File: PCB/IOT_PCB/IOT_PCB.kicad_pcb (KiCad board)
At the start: 2 copper layers, 6 parts, among them J1 Screw_Terminal_01x02, J2 Screw_Terminal_01x02, U1 ESP32-S3-WROOM-1, U2 BME280, U3 SCD41-D-R2

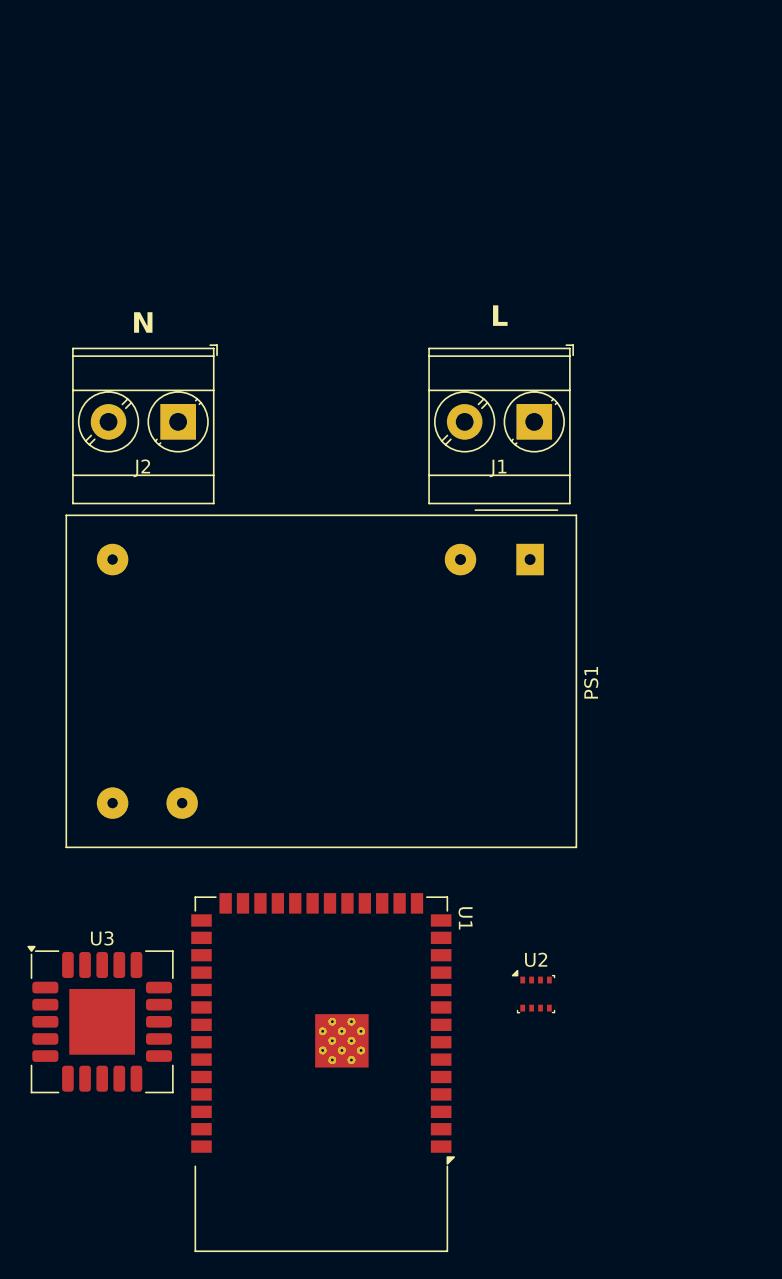
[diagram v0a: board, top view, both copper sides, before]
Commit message: Rough component placement and schematic WIP
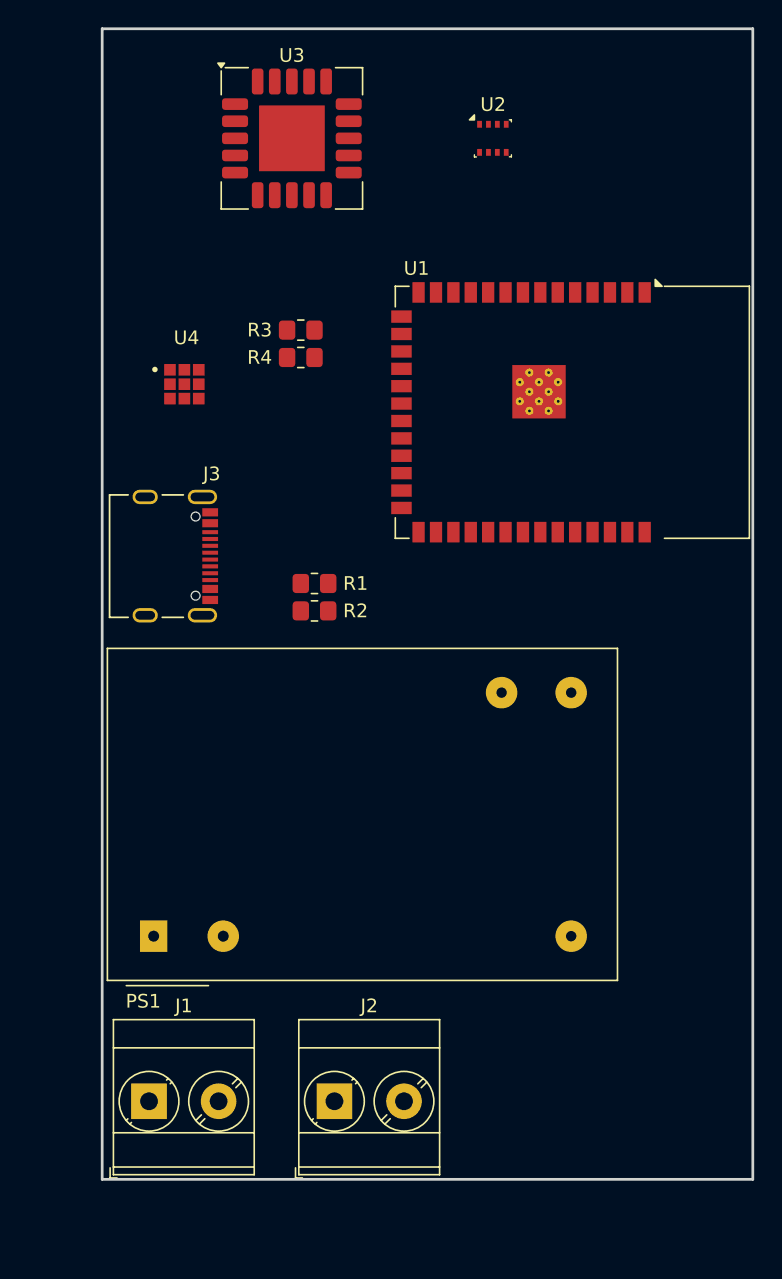
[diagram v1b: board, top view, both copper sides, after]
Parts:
- added J3: 10155435-00011LF USB-C, USBC_2 Amphenol 10155435-00011LF:AMPHENOL_10155435-00011LF, F.Cu at (87.1, 91.0)
- added R1: 5.1k, Resistor_SMD:R_0805_2012Metric_Pad1.20x1.40mm_HandSolder, F.Cu at (99.5, 93.0)
- added R2: 5.1k, Resistor_SMD:R_0805_2012Metric_Pad1.20x1.40mm_HandSolder, F.Cu at (99.5, 95.0)
- added R3: 22, Resistor_SMD:R_0805_2012Metric_Pad1.20x1.40mm_HandSolder, F.Cu at (98.5, 74.5)
- added R4: 22, Resistor_SMD:R_0805_2012Metric_Pad1.20x1.40mm_HandSolder, F.Cu at (98.5, 76.5)
- added U4: ENS160-BGLM, ENS160_BGLM:XDCR_ENS160-BGLM, F.Cu at (90.0, 78.5)
- moved U3 66.0 mm to (97.8, 60.5)
- moved U2 62.6 mm to (112.5, 60.5)
- moved J1 57.0 mm to (87.4, 130.8), turned to 0 degrees
- moved U1 51.7 mm to (118.3, 80.5), turned to -90 degrees
- moved J2 50.9 mm to (101.0, 130.8), turned to 0 degrees
- moved PS1 38.9 mm to (87.8, 118.7), turned to 90 degrees
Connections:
- PS1 pad 14: unconnected-(PS1--Vo-Pad14) -> GND
- PS1 pad 16: unconnected-(PS1-+Vo-Pad16) -> +3V3
- U1 pad 1: Net-(U1-GND-Pad1) -> GND
- U1 pad 13: unconnected-(U1-IO19-Pad13) -> /USB_D-
- U1 pad 14: unconnected-(U1-IO20-Pad14) -> /USB_D+
- U1 pad 2: unconnected-(U1-3V3-Pad2) -> +3V3
- U1 pad 40: Net-(U1-GND-Pad1) -> GND
- U1 pad 41: Net-(U1-GND-Pad1) -> GND
- U1 pad 6: unconnected-(U1-IO6-Pad6) -> /SDA
- U1 pad 7: unconnected-(U1-IO7-Pad7) -> /SCL
- U2 pad 1: unconnected-(U2-GND-Pad1) -> GND
- U2 pad 2: unconnected-(U2-CSB-Pad2) -> +3V3
- U2 pad 3: unconnected-(U2-SDI-Pad3) -> /SDA
- U2 pad 4: unconnected-(U2-SCK-Pad4) -> /SCL
- U2 pad 5: unconnected-(U2-SDO-Pad5) -> GND
- U2 pad 6: unconnected-(U2-VDDIO-Pad6) -> +3V3
- U2 pad 7: unconnected-(U2-GND-Pad7) -> GND
- U3 pad 10: unconnected-(U3-SDA-Pad10) -> /SDA
- U3 pad 20: Net-(U3-GND-Pad20) -> GND
- U3 pad 21: Net-(U3-GND-Pad20) -> GND
- U3 pad 6: Net-(U3-GND-Pad20) -> GND
- U3 pad 9: unconnected-(U3-SCL-Pad9) -> /SCL
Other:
- board outline added: 47.5 x 84 mm
- board text removed: "L"
- board text removed: "N"

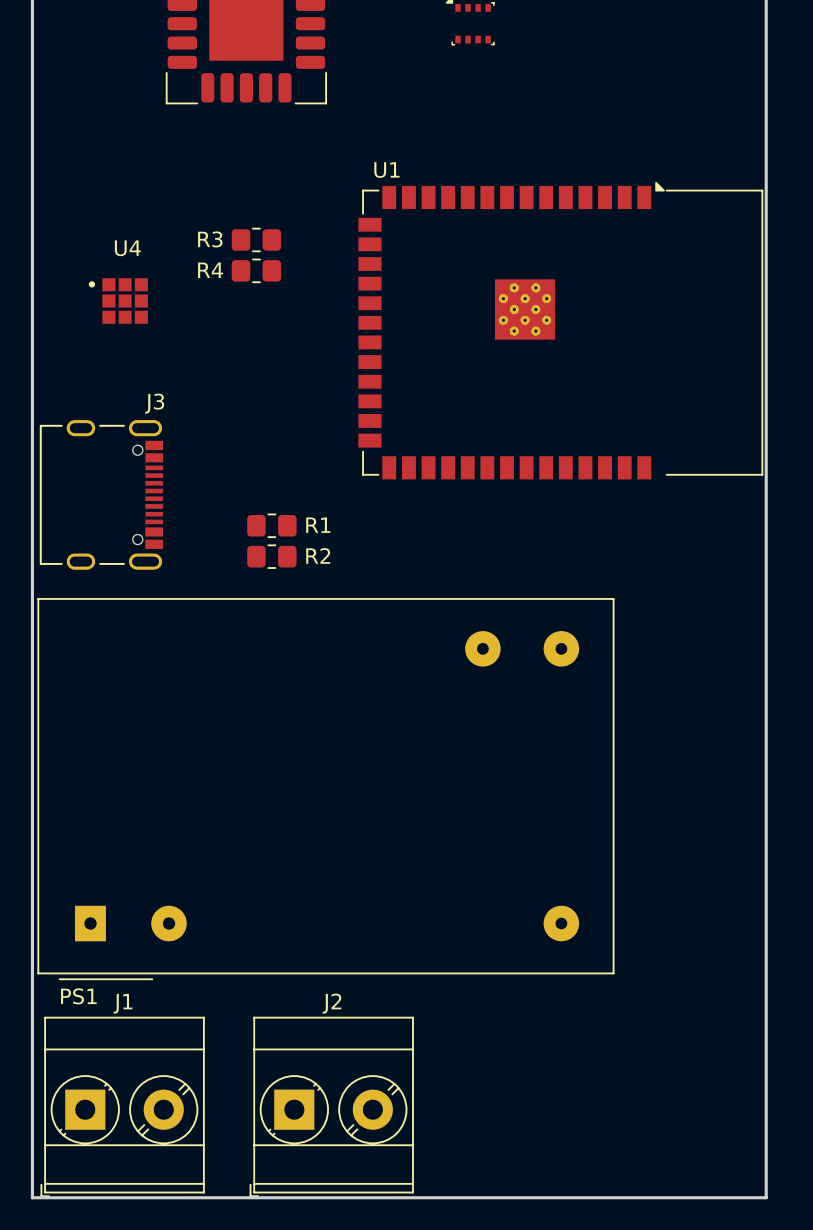
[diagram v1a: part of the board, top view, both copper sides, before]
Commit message: Changed IRM footprint to SMD
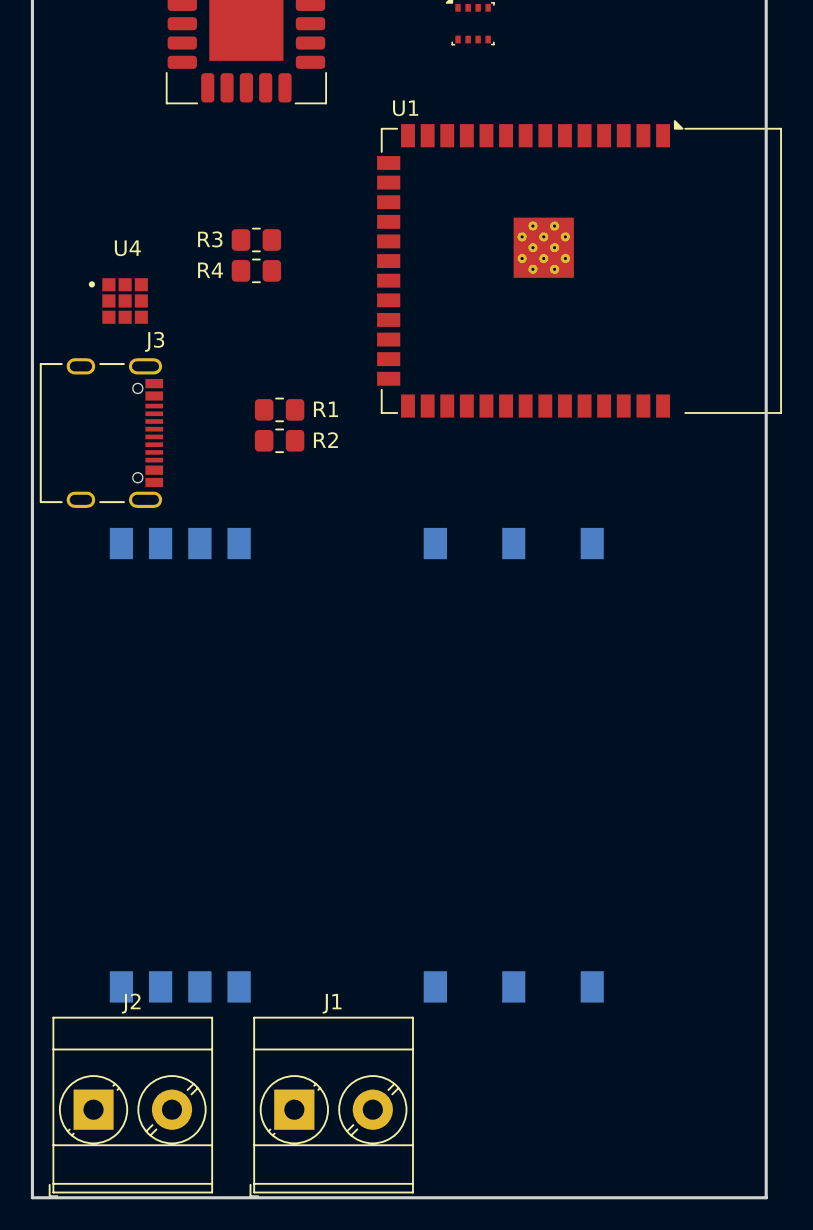
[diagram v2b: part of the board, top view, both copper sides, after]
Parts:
- PS1: value IRM-03-3.3 -> IRM-03-3.3S; footprint Converter_ACDC:Converter_ACDC_MeanWell_IRM-03-xx_THT -> Converter_ACDC:Converter_ACDC_MeanWell_IRM-03-xx_SMD; moved to B.Cu
- moved PS1 20.1 mm to (105.0, 108.5)
- moved J1 13.5 mm to (101.0, 130.8)
- moved J2 13.0 mm to (88.0, 130.8)
- moved R1 7.52 mm to (100.0, 85.5)
- moved R2 7.52 mm to (100.0, 87.5)
- moved U1 4.18 mm to (119.6, 76.5)
- moved J3 4.00 mm to (87.1, 87.0)
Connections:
- PS1 pad 5: unconnected-(PS1-NC-Pad5) -> (no net)

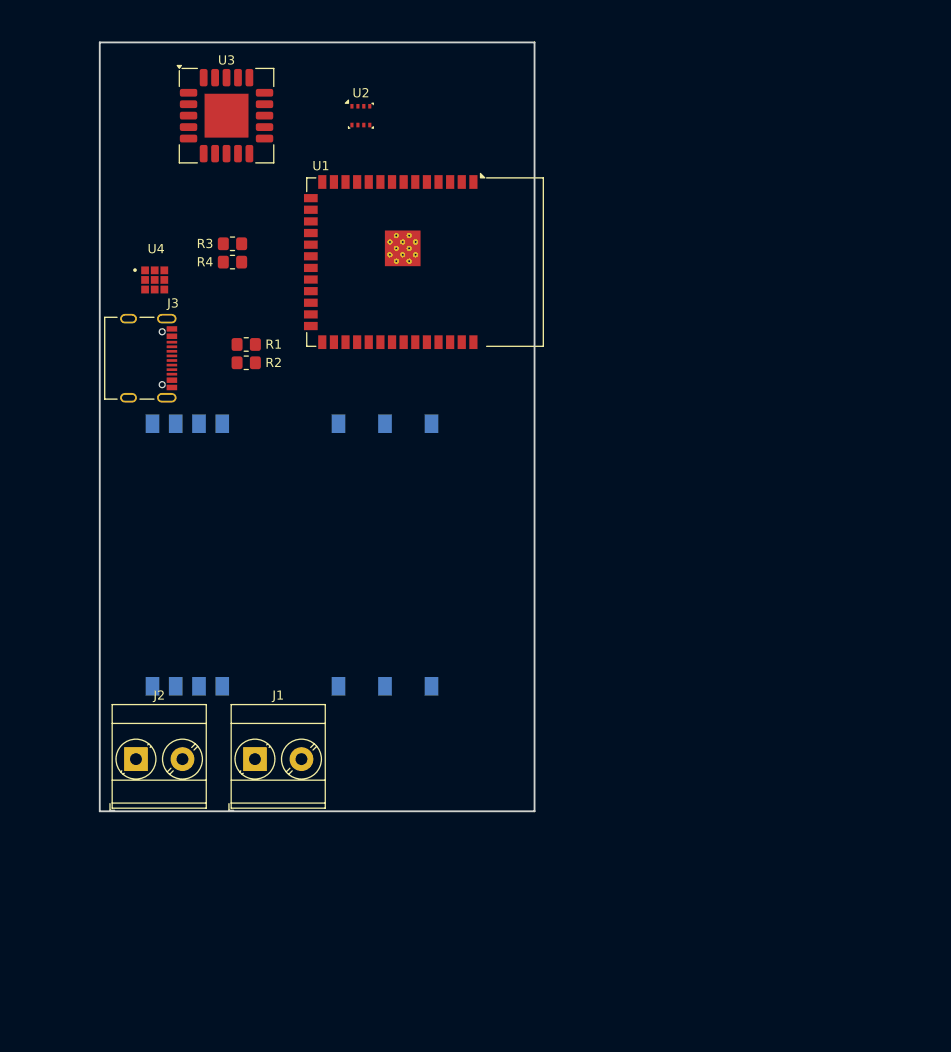
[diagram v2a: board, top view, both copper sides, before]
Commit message: Shrunk Board
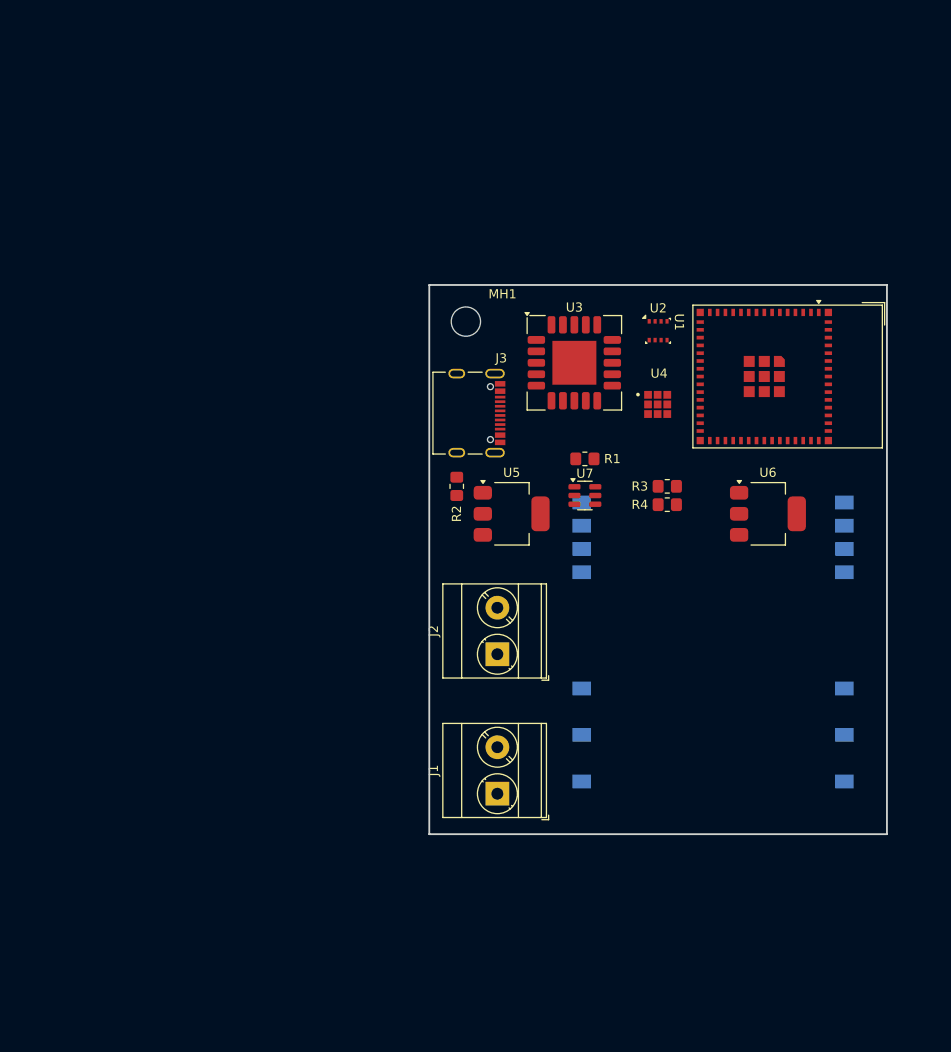
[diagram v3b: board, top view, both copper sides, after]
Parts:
- added MH1: MountingHole, MountingHole:MountingHole_3.2mm_M3, F.Cu at (124.0, 83.0)
- added U5: AMS1117-3.3, Package_TO_SOT_SMD:SOT-223-3_TabPin2, F.Cu at (129.0, 104.0)
- added U6: AMS1117-1.8, Package_TO_SOT_SMD:SOT-223-3_TabPin2, F.Cu at (157.0, 104.0)
- added U7: USBLC6-2SC6, Package_TO_SOT_SMD:SOT-23-6, F.Cu at (137.0, 102.0)
- U1: value ESP32-S3-WROOM-1 -> ESP32-S3-MINI-1; footprint RF_Module:ESP32-S3-WROOM-1 -> RF_Module:ESP32-S2-MINI-1
- moved U4 56.6 mm to (144.9, 92.0)
- moved R3 54.4 mm to (146.0, 101.0)
- moved R4 54.4 mm to (146.0, 103.0)
- moved PS1 47.0 mm to (151.0, 118.0), turned to 0 degrees
- moved U3 46.6 mm to (135.8, 87.5)
- moved U1 41.5 mm to (159.2, 89.0)
- moved J2 41.1 mm to (127.4, 119.3), turned to 90 degrees
- moved U2 40.1 mm to (145.0, 84.0)
- moved R1 39.1 mm to (137.0, 98.0)
- moved J3 36.4 mm to (123.0, 93.0)
- moved J1 26.8 mm to (127.4, 134.6), turned to 90 degrees
- moved R2 26.7 mm to (123.0, 101.0), turned to -90 degrees
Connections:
- R3 pad 1: Net-(J3-DN1) -> Net-(R3-Pad1)
- R4 pad 1: Net-(J3-DP1) -> Net-(R4-Pad1)
- U1 pad 10: unconnected-(U1-IO17-Pad10) -> /SDA
- U1 pad 11: unconnected-(U1-IO18-Pad11) -> /SCL
- U1 pad 13: /USB_D- -> unconnected-(U1-IO9-Pad13)
- U1 pad 14: /USB_D+ -> unconnected-(U1-IO10-Pad14)
- U1 pad 2: +3V3 -> GND
- U1 pad 23: unconnected-(U1-IO21-Pad23) -> /USB_D-
- U1 pad 24: unconnected-(U1-IO47-Pad24) -> /USB_D+
- U1 pad 3: unconnected-(U1-EN-Pad3) -> +3V3
- U1 pad 40: GND -> unconnected-(U1-RXD0-Pad40)
- U1 pad 41: GND -> unconnected-(U1-IO45-Pad41)
- U1 pad 6: /SDA -> unconnected-(U1-IO2-Pad6)
- U1 pad 7: /SCL -> unconnected-(U1-IO3-Pad7)
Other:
- board size 47.5 x 84 mm -> 50 x 60 mm

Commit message: Power mannagement
Changed to beefier 5V supply instead of 3V3. Combined 5V supply with USB using diodes. Added caps and fuses.
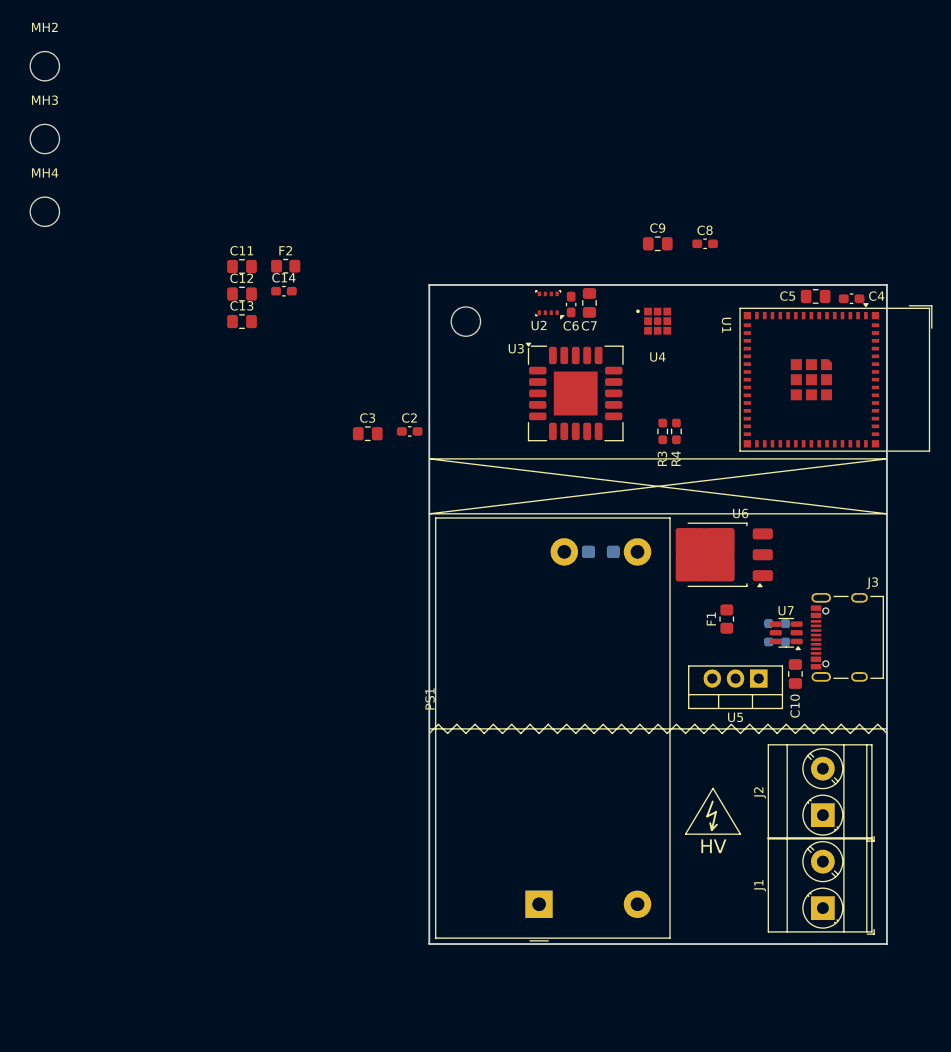
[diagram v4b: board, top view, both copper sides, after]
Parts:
- added C1: 100µF, Capacitor_Tantalum_SMD:CP_EIA-3216-12_Kemet-S, B.Cu at (138.8, 108.2)
- added C10: 1µF, Capacitor_SMD:C_0805_2012Metric_Pad1.18x1.45mm_HandSolder, F.Cu at (160.0, 121.5)
- added C11: 10µF, Capacitor_SMD:C_0805_2012Metric_Pad1.18x1.45mm_HandSolder, F.Cu at (99.5, 77.0)
- added C12: 1µF, Capacitor_SMD:C_0805_2012Metric_Pad1.18x1.45mm_HandSolder, F.Cu at (99.5, 80.0)
- added C13: 1µF, Capacitor_SMD:C_0805_2012Metric_Pad1.18x1.45mm_HandSolder, F.Cu at (99.5, 83.0)
- added C14: 0.1µF, Capacitor_SMD:C_0603_1608Metric_Pad1.08x0.95mm_HandSolder, F.Cu at (104.1, 79.7)
- added C2: 0.1µF, Capacitor_SMD:C_0603_1608Metric_Pad1.08x0.95mm_HandSolder, F.Cu at (117.9, 95.0)
- added C3: 1µF, Capacitor_SMD:C_0805_2012Metric_Pad1.18x1.45mm_HandSolder, F.Cu at (113.3, 95.2)
- added C4: 0.1µF, Capacitor_SMD:C_0603_1608Metric_Pad1.08x0.95mm_HandSolder, F.Cu at (166.1, 80.5)
- added C5: 10µF, Capacitor_SMD:C_0805_2012Metric_Pad1.18x1.45mm_HandSolder, F.Cu at (162.2, 80.2)
- added C6: 0.1µF, Capacitor_SMD:C_0603_1608Metric_Pad1.08x0.95mm_HandSolder, F.Cu at (135.5, 81.1)
- added C7: 1µF, Capacitor_SMD:C_0805_2012Metric_Pad1.18x1.45mm_HandSolder, F.Cu at (137.5, 81.0)
- added C8: 0.1µF, Capacitor_SMD:C_0603_1608Metric_Pad1.08x0.95mm_HandSolder, F.Cu at (150.1, 74.5)
- added C9: 1µF, Capacitor_SMD:C_0805_2012Metric_Pad1.18x1.45mm_HandSolder, F.Cu at (145.0, 74.5)
- added F1: Polyfuse, Resistor_SMD:R_0805_2012Metric_Pad1.20x1.40mm_HandSolder, F.Cu at (152.5, 115.5)
- added F2: Polyfuse, Resistor_SMD:R_0805_2012Metric_Pad1.20x1.40mm_HandSolder, F.Cu at (104.3, 77.0)
- added MH2: MountingHole, MountingHole:MountingHole_3.2mm_M3, F.Cu at (78.0, 55.1)
- added MH3: MountingHole, MountingHole:MountingHole_3.2mm_M3, F.Cu at (78.0, 63.0)
- added MH4: MountingHole, MountingHole:MountingHole_3.2mm_M3, F.Cu at (78.0, 71.0)
- J1, J2: value Screw_Terminal_01x02 -> Screw_Terminal
- J3: value 10155435-00011LF USB-C -> USB-C Conn
- PS1: value IRM-03-3.3S -> IRM-05-5; footprint Converter_ACDC:Converter_ACDC_MeanWell_IRM-03-xx_SMD -> Converter_ACDC:Converter_ACDC_MeanWell_IRM-05-xx_THT; moved to F.Cu
- R1, R2: value 5.1k -> 5.1kΩ; footprint Resistor_SMD:R_0805_2012Metric_Pad1.20x1.40mm_HandSolder -> Resistor_SMD:R_0603_1608Metric_Pad0.98x0.95mm_HandSolder; moved to B.Cu
- R3, R4: value 22 -> 22Ω; footprint Resistor_SMD:R_0805_2012Metric_Pad1.20x1.40mm_HandSolder -> Resistor_SMD:R_0603_1608Metric_Pad0.98x0.95mm_HandSolder
- U5: value AMS1117-3.3 -> 3V3 Reg; footprint Package_TO_SOT_SMD:SOT-223-3_TabPin2 -> Package_TO_SOT_THT:TO-220-3_Vertical
- U6: value AMS1117-1.8 -> 1V8 Reg; footprint Package_TO_SOT_SMD:SOT-223-3_TabPin2 -> Package_TO_SOT_SMD:TO-252-3_TabPin2
- U7: value USBLC6-2SC6 -> ESD Suppresion
- moved J3 50.4 mm to (167.0, 117.5), turned to 90 degrees
- moved J2 39.7 mm to (163.0, 136.9)
- moved R2 38.1 mm to (158.0, 116.0), turned to 0 degrees
- moved J1 37.7 mm to (163.0, 147.1)
- moved PS1 34.4 mm to (132.0, 146.7), turned to 90 degrees
- moved U5 32.4 mm to (156.0, 122.0), turned to 180 degrees
- moved R1 29.0 mm to (158.0, 118.0)
- moved U7 26.6 mm to (159.0, 117.0), turned to 180 degrees
- moved U2 12.4 mm to (133.0, 81.0), turned to 180 degrees
- moved U4 9.10 mm to (144.9, 83.0)
- moved R4 8.06 mm to (147.0, 95.0), turned to 90 degrees
- moved U6 7.17 mm to (151.4, 108.5), turned to 180 degrees
- moved R3 6.02 mm to (145.5, 95.0), turned to 90 degrees
- moved U1 5.16 mm to (164.3, 89.3)
- moved U3 3.35 mm to (136.0, 90.8)
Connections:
- PS1 pad 1: AC_L -> AC_N
- PS1 pad 3: AC_N -> GND
- U5 pad 2: unconnected-(U5-VO-Pad2) -> +3V3
- U5 pad 3: unconnected-(U5-VI-Pad3) -> +5V
- U6 pad 2: unconnected-(U6-VO-Pad2) -> +1V8
- U6 pad 3: unconnected-(U6-VI-Pad3) -> +5V
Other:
- board size 50 x 60 mm -> 50 x 72 mm
- board text added: "HV"
